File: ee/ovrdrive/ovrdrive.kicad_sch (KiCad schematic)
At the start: 49 parts, among them J1 USB_A, J3 Conn_02x03_Counter_Clockwise, Q1 SSM3J328R,LF, Q2 SSM3J328R,LF, Q3 DMG1012TQ-7, U1 SM3257ENT, U2 FLASH, U3 ATtiny24A-MM, U4 SN74LVC1G32DCKR, U5 DRV8837C

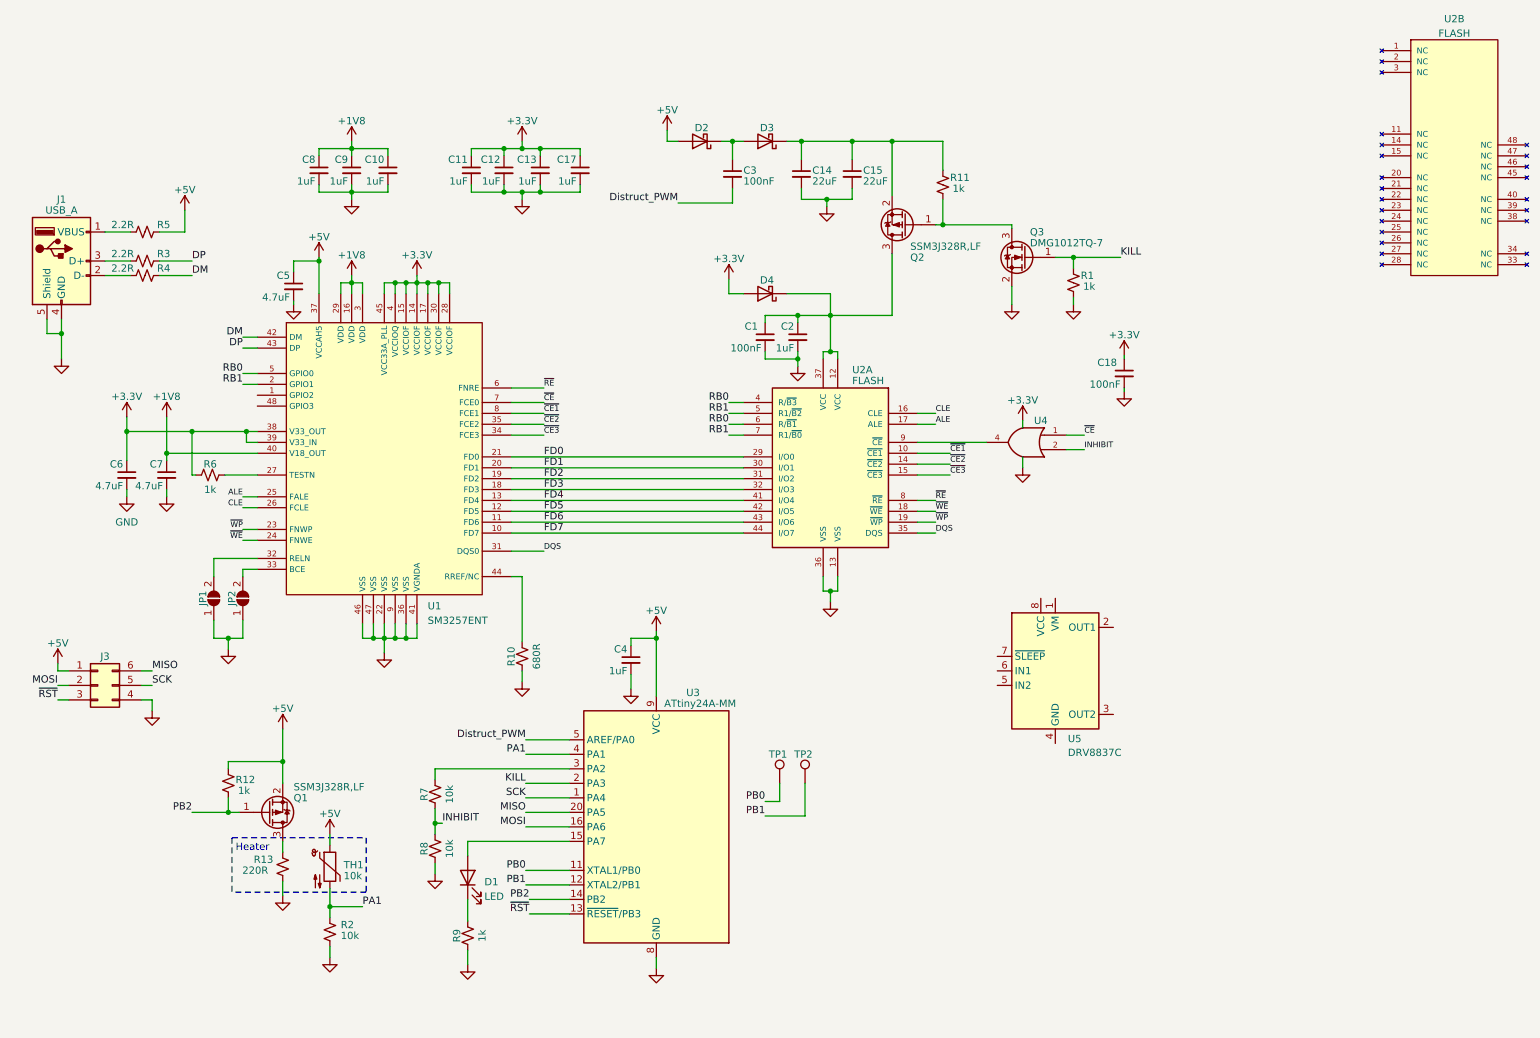
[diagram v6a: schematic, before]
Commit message: Change the destruction circuit to an H-bridge.
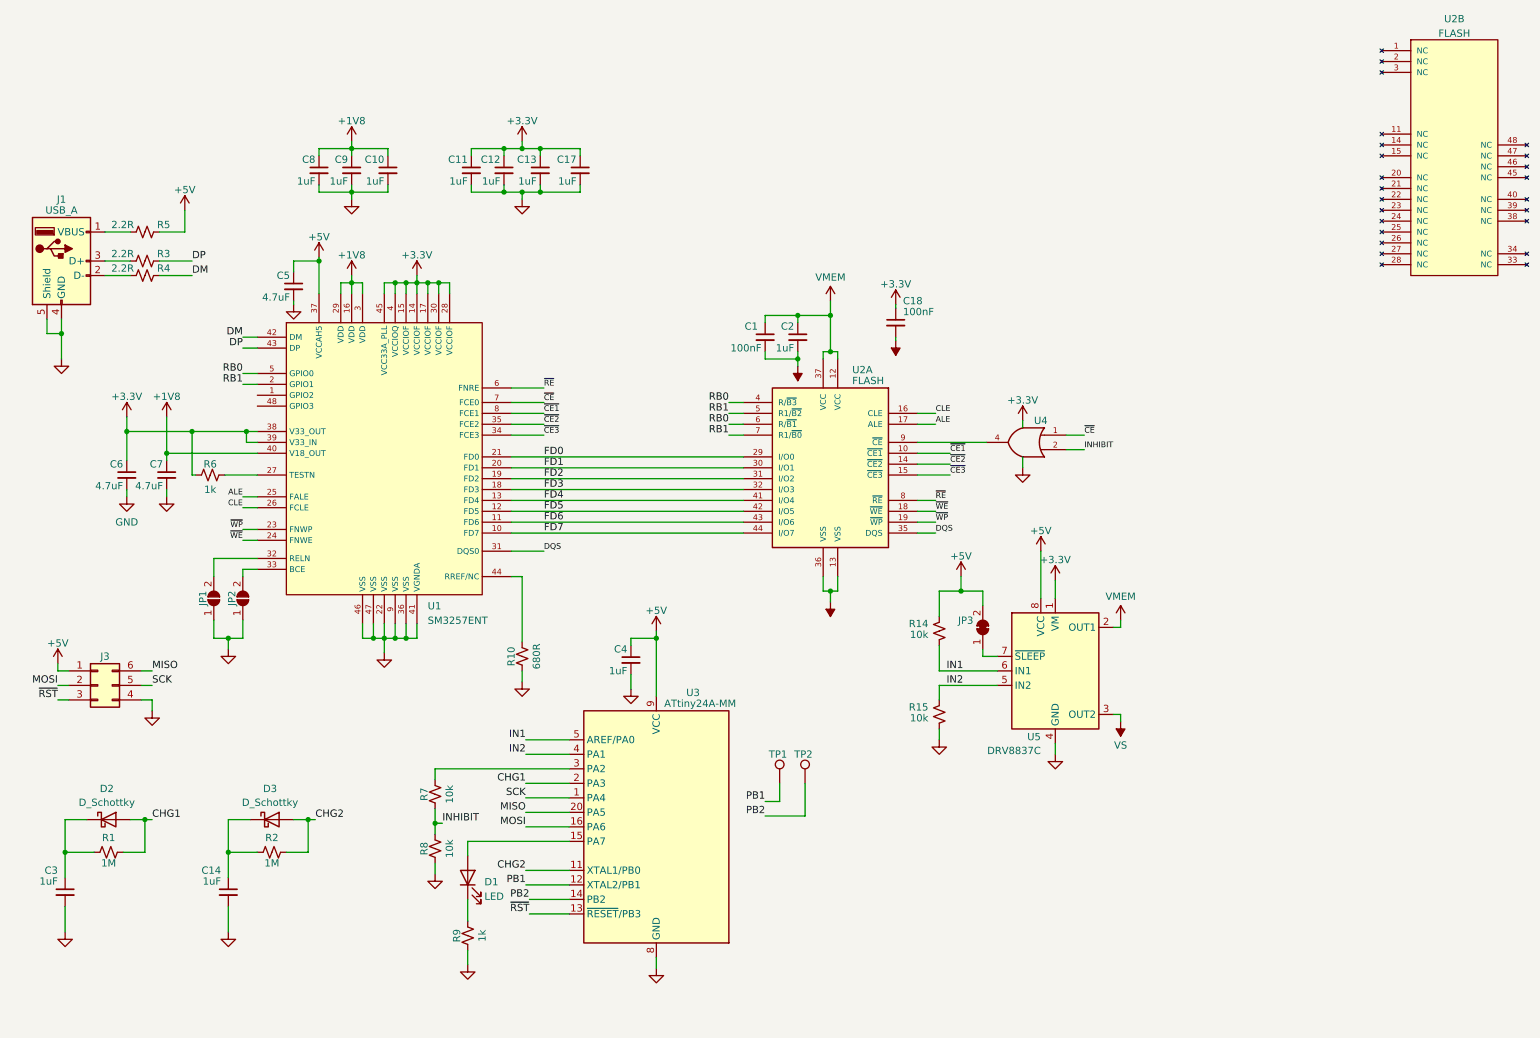
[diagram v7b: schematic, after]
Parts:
- removed C15: 22uF, Capacitor_SMD:C_0603_1608Metric, symbol Device:C_Small
- removed D4: D_Schottky, Diode_SMD:D_0603_1608Metric, symbol Device:D_Schottky
- removed Q1, Q2: SSM3J328R,LF, Package_TO_SOT_SMD:SOT-23, symbol Device:Q_PMOS_GSD
- removed Q3: DMG1012TQ-7, Package_TO_SOT_SMD:SOT-523, symbol Device:Q_NMOS_GSD
- removed R11, R12: 1k, Resistor_SMD:R_0402_1005Metric, symbol Device:R_Small_US
- removed R13: 220R, Resistor_SMD:R_0603_1608Metric, symbol Device:R_Small_US
- removed TH1: 10k, Resistor_SMD:R_0603_1608Metric, symbol Device:Thermistor_NTC
- added JP3: SolderJumper_2_Bridged, symbol Jumper:SolderJumper_2_Bridged
- added R14, R15: 10k, Resistor_SMD:R_0402_1005Metric, symbol Device:R_Small_US
- C14: value 22uF -> 1uF; MPN CL10A226MO7JZNC -> (none)
- C3: value 100nF -> 1uF; MPN CC0603KRX7R7BB104 -> (none)
- D2, D3: footprint Diode_SMD:D_0603_1608Metric -> (none); MPN CD0603-B0340R -> (none)
- R1: value 1k -> 1M; footprint Resistor_SMD:R_0402_1005Metric -> (none); MPN RC0402FR-071KL -> (none)
- R2: value 10k -> 1M; footprint Resistor_SMD:R_0402_1005Metric -> (none); MPN RC0402FR-0710KL -> (none)
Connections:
- net +3.3V: now also U5.1 (VM)
- net +5V: now also U5.8 (VCC), JP3.2 (B), R14.2; no longer D2.2 (A)
- net GND: now also C3.2, U5.4 (GND), U5.9 (GND), R15.1; no longer C1.2, C18.2, C2.2, R1.1, R2.1, U2.13 (VSS), U2.36 (VSS)
- net PB1: now also TP1.1; no longer TP2.1
- net PB2: now also TP2.1
- net at C14.1, D3.1 (K): now also R2.2
- net at C3.1, D2.1 (K): now also R1.2; no longer D3.2 (A)
- net VMEM: now reaches C1.1, C2.1, U2.12 (VCC), U2.37 (VCC)
- net VMEM: now also U5.2 (OUT1)
- net VS: now reaches U5.3 (OUT2)
- net VS: now also C1.2, C18.2, C2.2, U2.13 (VSS), U2.36 (VSS)
- net IN2: now reaches U5.5 (IN2)
- net IN2: now also U3.4 (PA1), R15.2
- net IN1: now reaches U5.6 (IN1)
- net IN1: now also U3.5 (AREF/PA0), R14.1
- net at U5.7 (~{SLEEP}): now also JP3.1 (A)
- removed net Distruct_PWM: C3.2, U3.5 (AREF/PA0)
- net KILL renamed CHG1
- net CHG1: now also D2.2 (A), R1.1; no longer R1.2
- removed net PA1: R2.2, U3.4 (PA1)
- net PB0 renamed CHG2
- net CHG2: now also D3.2 (A), R2.1; no longer TP1.1
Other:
- note removed: "Heater"
- moved on the sheet: C18

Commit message: Started the routing the new H-bridge.
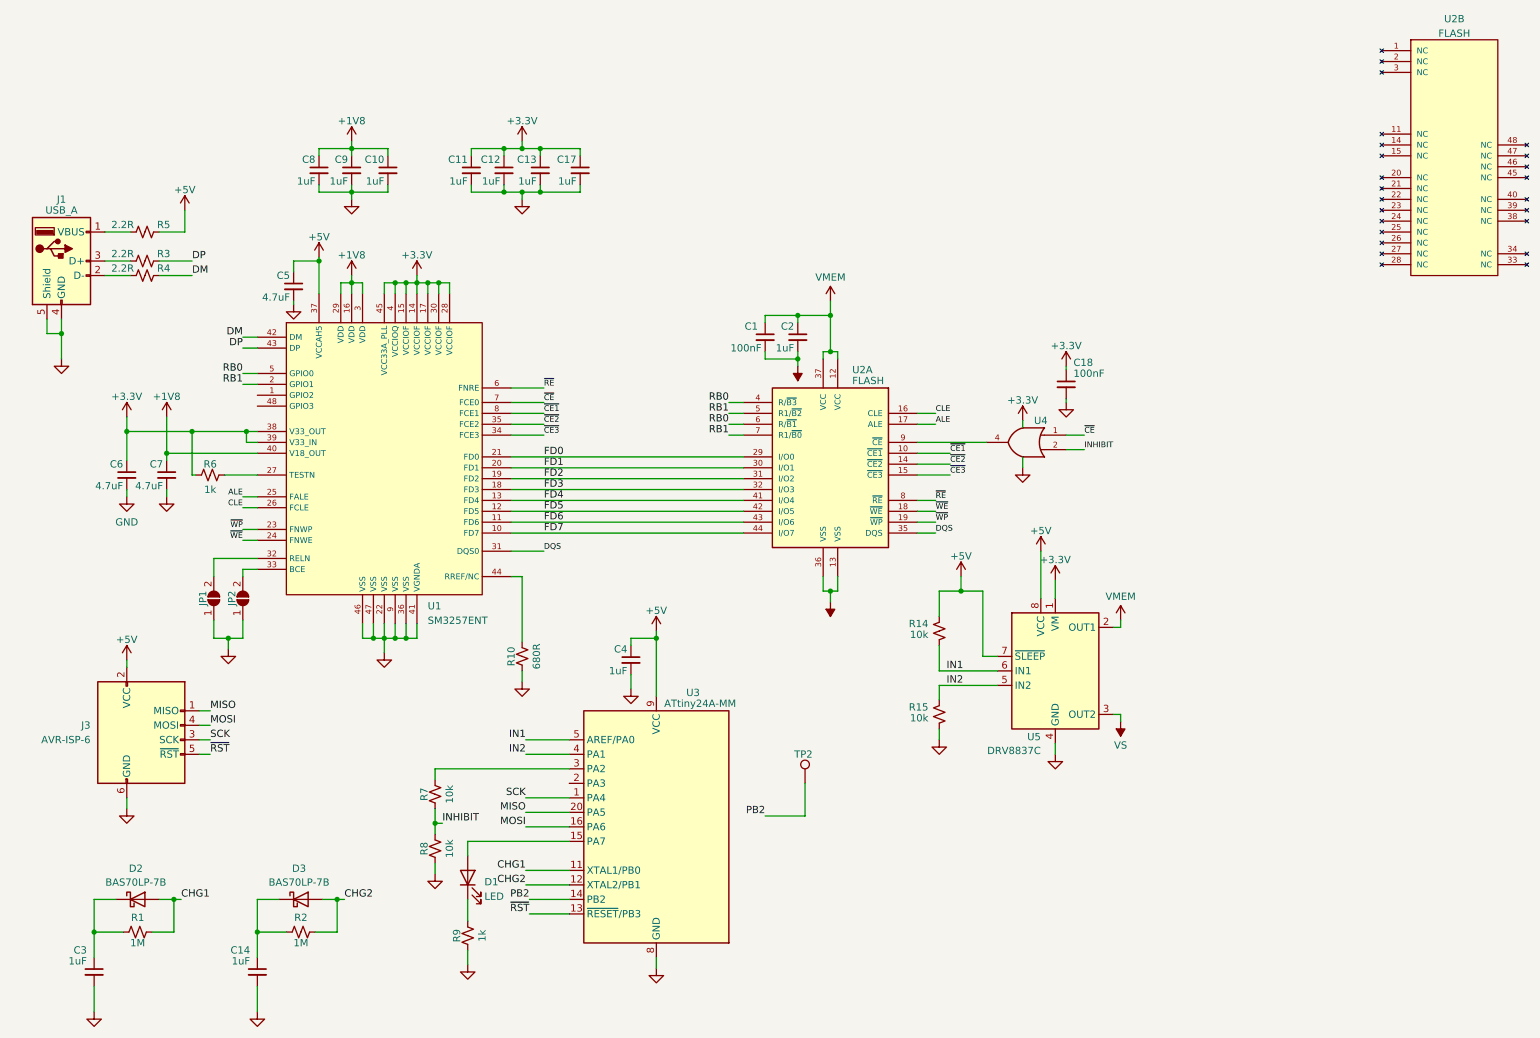
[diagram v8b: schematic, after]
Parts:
- removed J3: Conn_02x03_Counter_Clockwise, Connector_PinHeader_1.27mm:PinHeader_2x03_P1.27mm_Horizontal, symbol Connector_Generic:Conn_02x03_Counter_Clockwise
- removed JP3: SolderJumper_2_Bridged, symbol Jumper:SolderJumper_2_Bridged
- removed TP1: TestPoint, TestPoint:TestPoint_Pad_D1.0mm, symbol Connector:TestPoint
- added J3: AVR-ISP-6, Connector_PinHeader_1.27mm:PinHeader_2x03_P1.27mm_Horizontal, symbol Connector:AVR-ISP-6
- D2, D3: value D_Schottky -> BAS70LP-7B; footprint (none) -> Diode_SMD:D_0402_1005Metric; MPN (none) -> BAS70LP-7B
- R1, R2: footprint (none) -> Resistor_SMD:R_0402_1005Metric
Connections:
- net PB1 is gone; now on net CHG2: U3.12 (XTAL2/PB1)
- net +5V: now also U5.7 (~{SLEEP}), J3.2 (VCC)
- net CHG1: now also U3.11 (XTAL1/PB0); no longer U3.2 (PA3)
- net CHG2: no longer U3.11 (XTAL1/PB0)
- net GND: now also C18.2, J3.6 (GND)
- net MISO: now also J3.1 (MISO)
- net MOSI: now also J3.4 (MOSI)
- net SCK: now also J3.3 (SCK)
- net VS: no longer C18.2
- net ~{RST}: now also J3.5 (~{RST})
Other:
- moved on the sheet: C14, C18, C3, D2, D3, R1, R2
